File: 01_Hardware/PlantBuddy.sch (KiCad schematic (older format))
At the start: 38 parts, among them J101 Debug, J102 NFC Antenna, J2 Conn_I2C_SDA, J3 Conn_I2C_SCL, Q101 AO3401A, U101 nRF52832-QFxx, U102 LTR-303ALS-01, U6 SHTC3, Y1 32MHz, Y2 32kHz

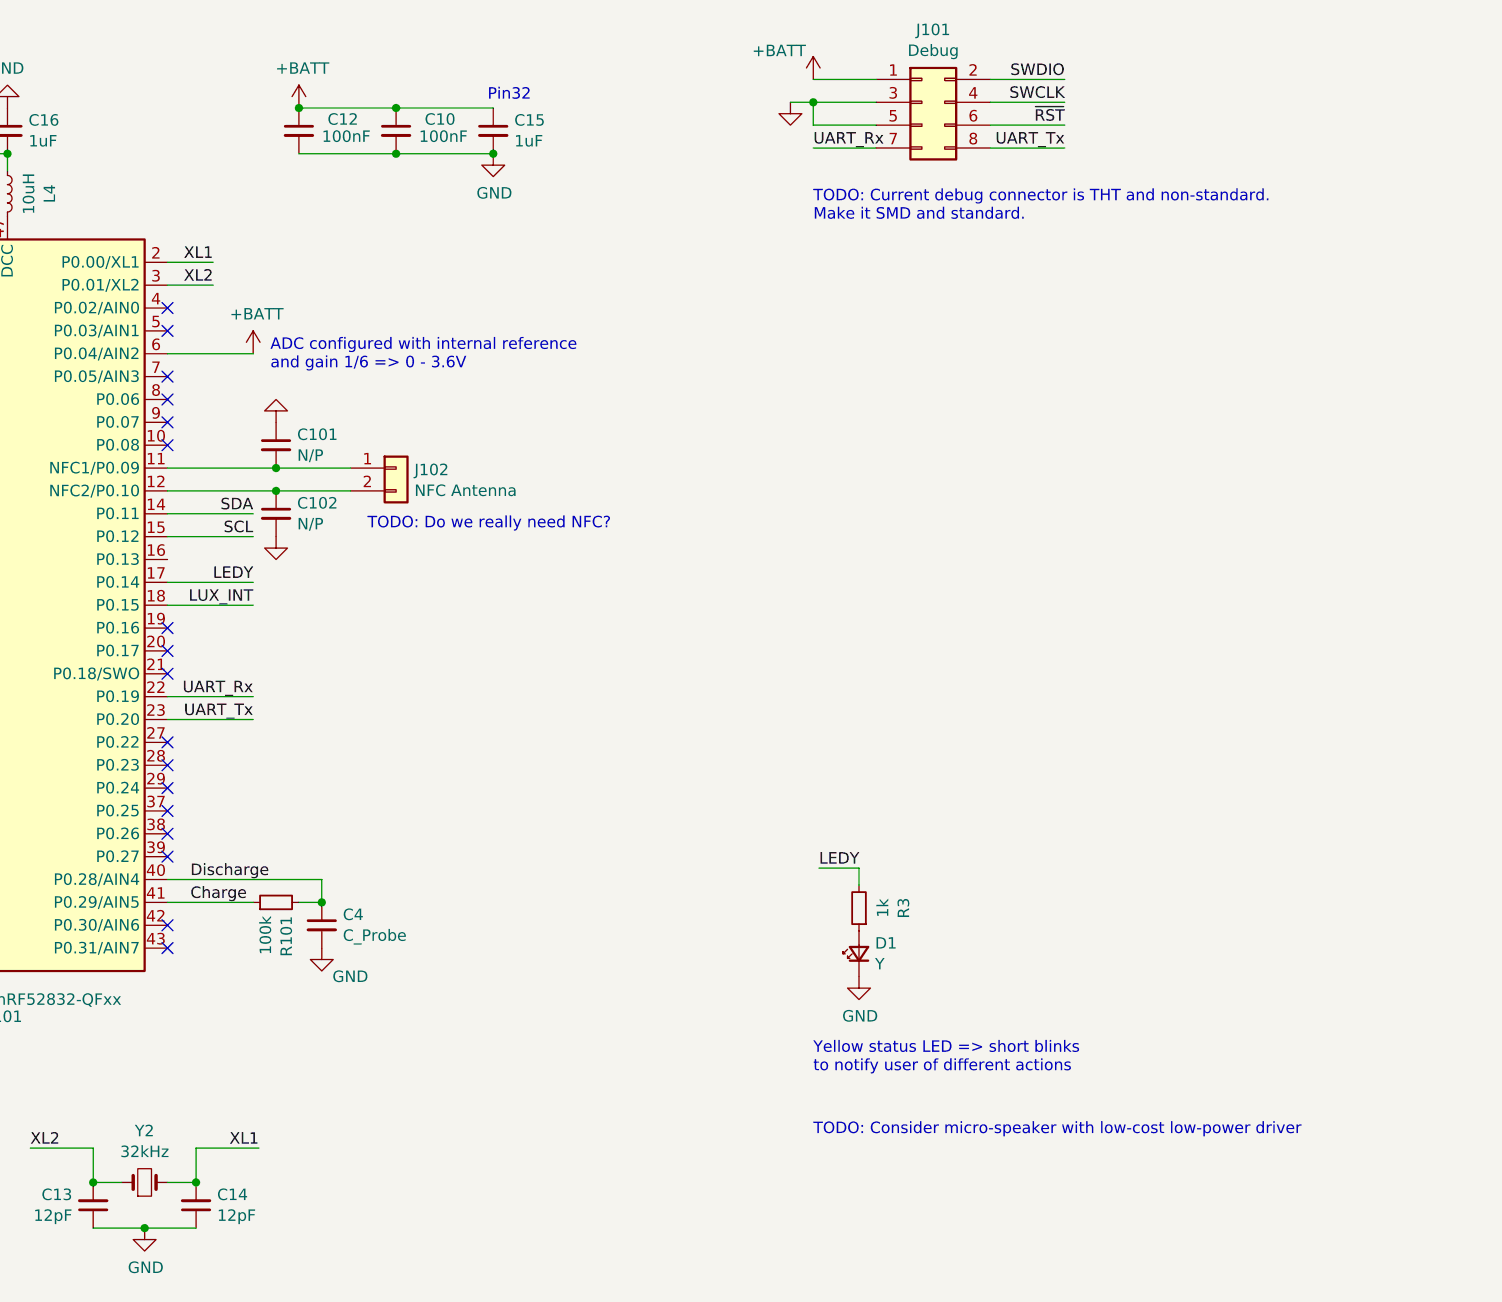
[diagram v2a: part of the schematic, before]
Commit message: Added new debug connector for J-Link.
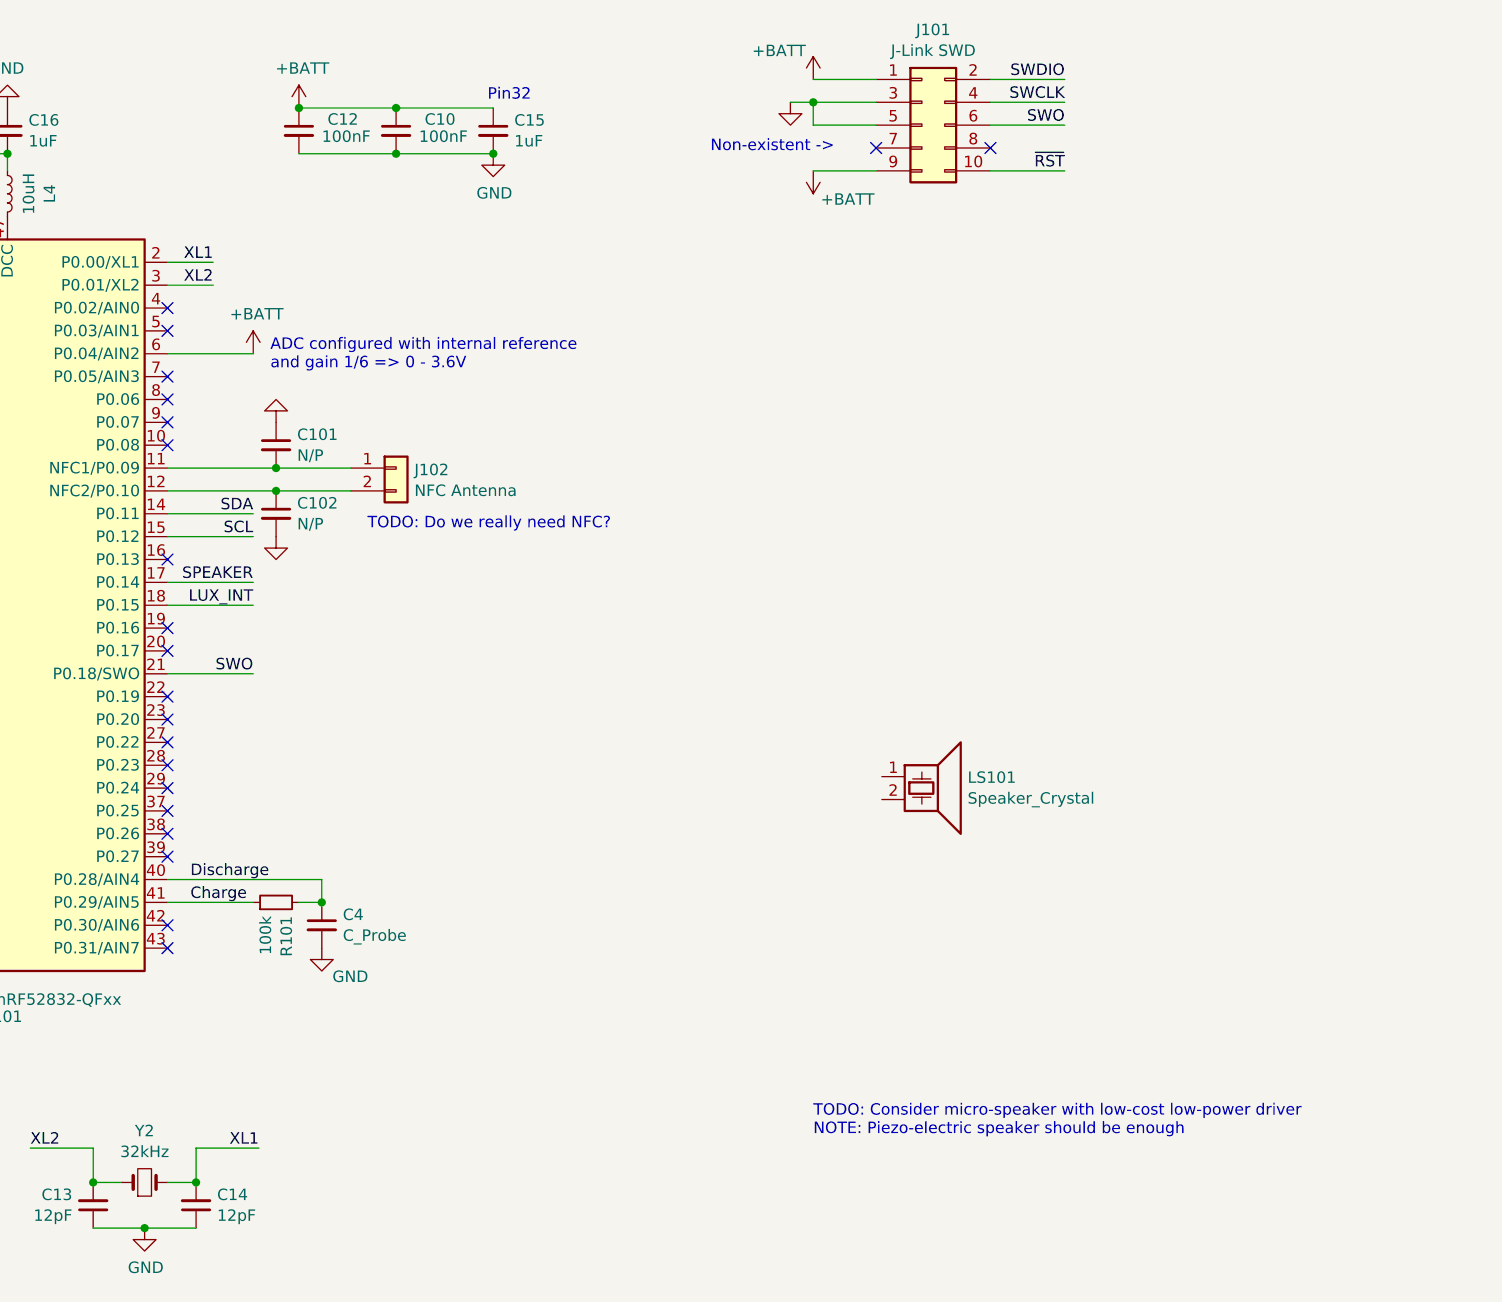
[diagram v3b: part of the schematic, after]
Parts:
- removed D1: Y, LED_SMD:LED_0603_1608Metric, symbol PlantBuddy-rescue:LED_Small-Device
- removed J101: Debug, PlantBuddy:PinHeader_2x04_P1.27mm_Vertical, symbol Connector_Generic:Conn_02x04_Odd_Even
- removed R3: 1k, Resistor_SMD:R_0402_1005Metric, symbol PlantBuddy-rescue:R_Small-Device
- added J101: J-Link SWD, Connector_PinHeader_1.27mm:PinHeader_2x05_P1.27mm_Vertical_SMD, symbol Connector_Generic:Conn_02x05_Odd_Even
- added LS101: Speaker_Crystal, symbol Device:Speaker_Crystal
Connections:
- net +BATT: now also J101.1 (Pin_1), J101.9 (Pin_9)
- net GND: now also J101.3 (Pin_3), J101.5 (Pin_5)
- net SWCLK: now also J101.4 (Pin_4)
- net SWDIO: now also J101.2 (Pin_2)
- net ~RST: now also J101.10 (Pin_10)
- net SWO: now reaches U101.21 (P0.18/SWO)
- net SWO: now also J101.6 (Pin_6)
- net LEDY renamed SPEAKER
- net UART_Rx: no longer names the net of U101.22 (P0.19)
- net UART_Tx: no longer names the net of U101.23 (P0.20)
- no-connect marks 20 -> 24
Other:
- note added: "Non-existent ->"
- note added: "TODO: Consider micro-speaker with low-cost low-power driver\nNOTE: Piezo-electric speaker should be enough"
- note removed: "TODO: Consider micro-speaker with low-cost low-power driver"
- note removed: "TODO: Current debug connector is THT and non-standard.\nMake it SMD and standard."
- note removed: "Yellow status LED => short blinks\nto notify user of different actions"
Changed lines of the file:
@@
 Text Notes 2825 7675 0    50   ~ 0
 Reverse-voltage protection
-Text Notes 9825 5225 0    50   ~ 0
-Yellow status LED => short blinks\nto notify user of different actions
 $Comp
 L PlantBuddy-rescue:Conn_01x01-Connector_Generic J3
@@
 $EndComp
 $Comp
-L PlantBuddy-rescue:LED_Small-Device D1
-U 1 1 5FC270B5
-P 10025 4700
-F 0 "D1" V 10071 4630 50  0000 R CNN
-F 1 "Y" V 9980 4630 50  0000 R CNN
-F 2 "LED_SMD:LED_0603_1608Metric" V 10025 4700 50  0001 C CNN
-F 3 "~" V 10025 4700 50  0001 C CNN
-F 4 "C72038" V 10025 4700 50  0001 C CNN "LCSC"
-	1    10025 4700
-	0    -1   -1   0
-$EndComp
-$Comp
-L PlantBuddy-rescue:GND-power #PWR01
-U 1 1 5FC2781D
-P 10025 4800
-F 0 "#PWR01" H 10025 4550 50  0001 C CNN
-F 1 "GND" H 10030 4627 50  0000 C CNN
-F 2 "" H 10025 4800 50  0001 C CNN
-F 3 "" H 10025 4800 50  0001 C CNN
-	1    10025 4800
-	1    0    0    -1
-$EndComp
-$Comp
-L PlantBuddy-rescue:R_Small-Device R3
-U 1 1 5FC33886
-P 10025 4500
-F 0 "R3" V 9829 4500 50  0000 C CNN
-F 1 "1k" V 9920 4500 50  0000 C CNN
-F 2 "Resistor_SMD:R_0402_1005Metric" H 10025 4500 50  0001 C CNN
-F 3 "~" H 10025 4500 50  0001 C CNN
-F 4 "C11702" V 10025 4500 50  0001 C CNN "LCSC"
-	1    10025 4500
-	-1   0    0    1
-$EndComp
-Wire Wire Line
-	10025 4400 10025 4325
-Wire Wire Line
-	10025 4325 9850 4325
-Text Label 9850 4325 0    50   ~ 0
-LEDY
-$Comp
 L PlantBuddy-rescue:C_Small-Device C17
 U 1 1 60156A34
@@
 Wire Wire Line
 	2875 7200 2875 7300
-Text Label 10925 1075 2    50   ~ 0
+Text Label 10925 1275 2    50   ~ 0
 ~RST
 Text Label 10925 875  2    50   ~ 0
@@
 	7375 3075 7000 3075
 Wire Wire Line
-	7375 3675 7000 3675
-Wire Wire Line
-	7375 3575 7000 3575
-Wire Wire Line
 	7000 2875 7375 2875
 Wire Wire Line
@@
 	-1   0    0    -1
 $EndComp
-Text Label 7375 3675 2    50   ~ 0
-UART_Tx
-Text Label 7375 3575 2    50   ~ 0
-UART_Rx
 Text Notes 7450 2150 0    50   ~ 0
 ADC configured with internal reference\nand gain 1/6 => 0 - 3.6V
@@
 	7375 3175 7000 3175
 Text Label 7375 3075 2    50   ~ 0
-LEDY
+SPEAKER
 Text Label 7375 3175 2    50   ~ 0
 LUX_INT
@@
 Wire Wire Line
 	10600 975  10925 975
-Text Label 10925 1175 2    50   ~ 0
-UART_Tx
-Wire Wire Line
-	10600 1175 10925 1175
-Wire Wire Line
-	10600 1075 10925 1075
+Wire Wire Line
+	10600 1275 10925 1275
 Wire Wire Line
 	7575 4475 7675 4475
@@
 NoConn ~ 7000 3875
 NoConn ~ 7000 3775
-NoConn ~ 7000 3475
 NoConn ~ 7000 3375
 NoConn ~ 7000 3275
@@
 F 3 "" H 9725 975 50  0001 C CNN
 	1    9725 975
-	1    0    0    -1
-$EndComp
-Text Label 9825 1175 0    50   ~ 0
-UART_Rx
-Wire Wire Line
-	9825 1175 10100 1175
-$Comp
-L Connector_Generic:Conn_02x04_Odd_Even J101
-U 1 1 6117791F
-P 10300 975
-F 0 "J101" H 10350 1292 50  0000 C CNN
-F 1 "Debug" H 10350 1201 50  0000 C CNN
-F 2 "PlantBuddy:PinHeader_2x04_P1.27mm_Vertical" H 10300 975 50  0001 C CNN
-F 3 "~" H 10300 975 50  0001 C CNN
-	1    10300 975
 	1    0    0    -1
 $EndComp
@@
 Wire Wire Line
 	2025 6850 1800 6850
-Text Notes 9825 1500 0    50   ~ 0
-TODO: Current debug connector is THT and non-standard.\nMake it SMD and standard.
 Text Notes 9825 5500 0    50   ~ 0
-TODO: Consider micro-speaker with low-cost low-power driver
+TODO: Consider micro-speaker with low-cost low-power driver\nNOTE: Piezo-electric speaker should be enough
 $Comp
 L PlantBuddy-rescue:Battery_Cell-Device BT1
@@
 	3325 7300 3725 7300
 Connection ~ 3325 7300
+Text Notes 7875 2850 0    50   ~ 0
+TODO: Do we really need NFC?
+Text Label 10925 1075 2    50   ~ 0
+SWO
+Wire Wire Line
+	10600 1075 10925 1075
+Text Label 7375 3475 2    50   ~ 0
+SWO
+Wire Wire Line
+	7375 3475 7000 3475
+$Comp
+L Connector_Generic:Conn_02x05_Odd_Even J101
+U 1 1 6136EE02
+P 10300 1075
+F 0 "J101" H 10350 1492 50  0000 C CNN
+F 1 "J-Link SWD" H 10350 1401 50  0000 C CNN
+F 2 "Connector_PinHeader_1.27mm:PinHeader_2x05_P1.27mm_Vertical_SMD" H 10300 1075 50  0001 C CNN
+F 3 "~" H 10300 1075 50  0001 C CNN
+	1    10300 1075
+	1    0    0    -1
+$EndComp
+NoConn ~ 10600 1175
+NoConn ~ 10100 1175
+Text Notes 9375 1200 0    50   ~ 0
+Non-existent ->
+$Comp
+L PlantBuddy-rescue:+BATT-power #PWR0121
+U 1 1 6137FB50
+P 9825 1275
+F 0 "#PWR0121" H 9825 1125 50  0001 C CNN
+F 1 "+BATT" H 9675 1400 50  0000 C CNN
+F 2 "" H 9825 1275 50  0001 C CNN
+F 3 "" H 9825 1275 50  0001 C CNN
+	1    9825 1275
+	-1   0    0    1
+$EndComp
+Wire Wire Line
+	9825 1275 10100 1275
+NoConn ~ 7000 2975
+$Comp
+L Device:Speaker_Crystal LS101
+U 1 1 6138F133
+P 10325 3925
+F 0 "LS101" H 10500 3921 50  0000 L CNN
+F 1 "Speaker_Crystal" H 10500 3830 50  0000 L CNN
+F 2 "" H 10290 3875 50  0001 C CNN
+F 3 "~" H 10290 3875 50  0001 C CNN
+	1    10325 3925
+	1    0    0    -1
+$EndComp
+NoConn ~ 7000 3575
+NoConn ~ 7000 3675
 Wire Bus Line
 	2175 5325 2625 5325
 Wire Bus Line
 	2175 5325 2175 6650
-Text Notes 7875 2850 0    50   ~ 0
-TODO: Do we really need NFC?
 $EndSCHEMATC

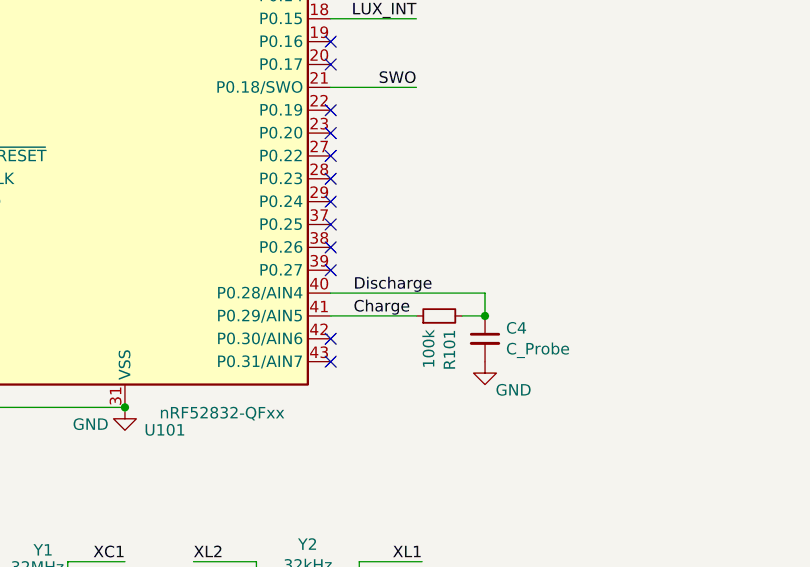
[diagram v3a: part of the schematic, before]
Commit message: PCB: Changed name of net.
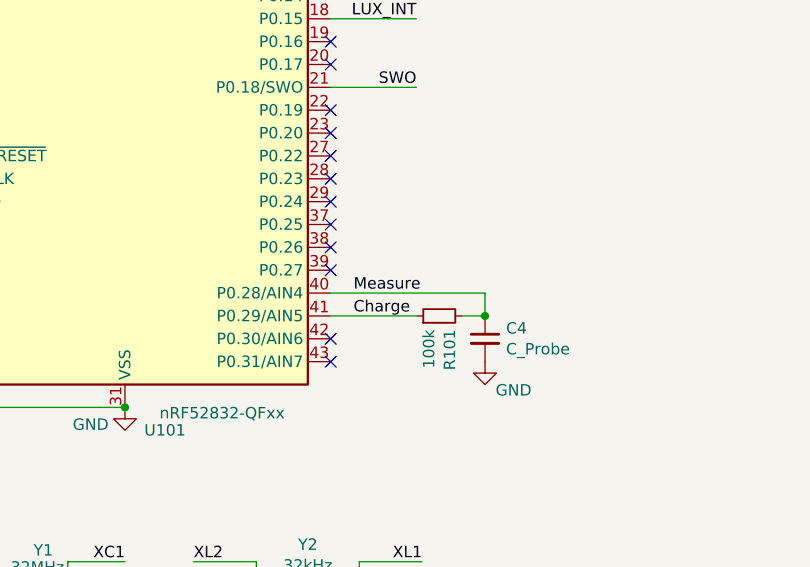
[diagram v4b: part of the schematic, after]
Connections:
- net Discharge renamed Measure
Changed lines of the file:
@@
 	7000 2775 7375 2775
 Text Label 7100 4375 0    50   ~ 0
-Discharge
+Measure
 Text Label 7100 4475 0    50   ~ 0
 Charge

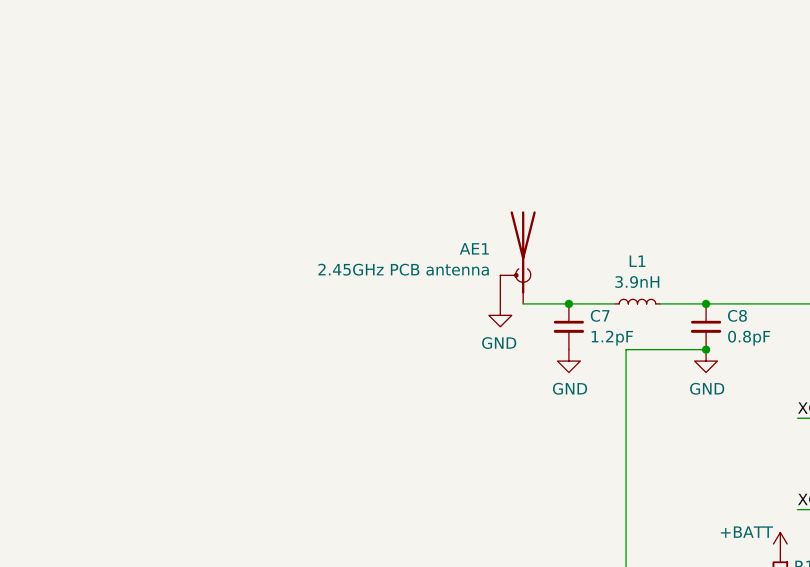
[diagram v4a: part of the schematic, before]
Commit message: Changed antenna design to monopole
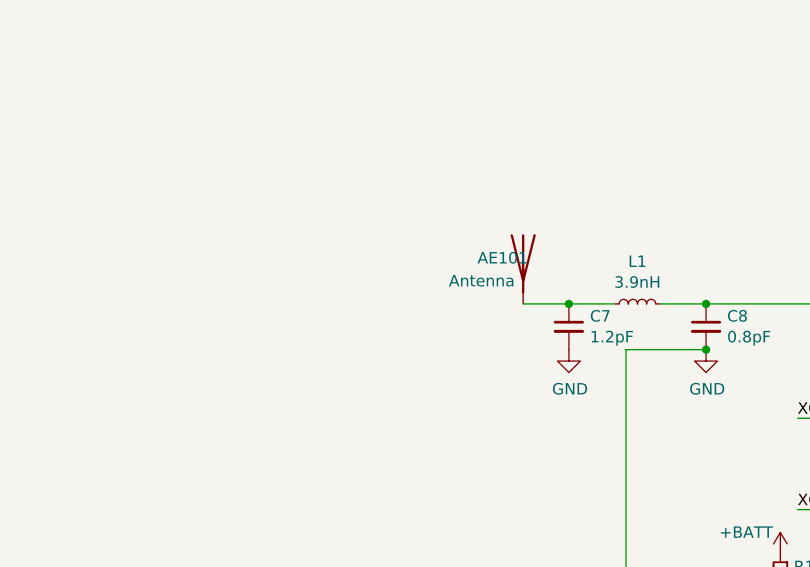
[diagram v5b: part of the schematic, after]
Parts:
- removed AE1: 2.45GHz PCB antenna, RF_Antenna:Texas_SWRA117D_2.4GHz_Right, symbol PlantBuddy-rescue:Antenna_Shield-Device
- added AE101: Antenna, PlantBuddy:monopole, symbol Device:Antenna
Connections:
- net at C7.1, L1.1: now also AE101.1 (A)
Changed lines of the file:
@@
-$EndComp
-$Comp
-L PlantBuddy-rescue:Antenna_Shield-Device AE1
-U 1 1 5F7B40C5
-P 3825 2275
-F 0 "AE1" H 3969 2314 50  0000 L CNN
-F 1 "2.45GHz PCB antenna" H 3969 2223 50  0000 L CNN
-F 2 "RF_Antenna:Texas_SWRA117D_2.4GHz_Right" H 3825 2375 50  0001 C CNN
-F 3 "~" H 3825 2375 50  0001 C CNN
-	1    3825 2275
-	-1   0    0    -1
 $EndComp
 $Comp
@@
 	1    7575 1000
 	1    0    0    -1
-$EndComp
-$Comp
-L PlantBuddy-rescue:GND-power #PWR038
-U 1 1 5F8EDD3C
-P 3725 2475
-F 0 "#PWR038" H 3725 2225 50  0001 C CNN
-F 1 "GND" H 3730 2302 50  0000 C CNN
-F 2 "" H 3725 2475 50  0001 C CNN
-F 3 "" H 3725 2475 50  0001 C CNN
-	1    3725 2475
-	-1   0    0    -1
 $EndComp
 Wire Wire Line
@@
 NoConn ~ 7000 3575
 NoConn ~ 7000 3675
+$Comp
+L Device:Antenna AE101
+U 1 1 613B6725
+P 3825 2275
+F 0 "AE101" H 3625 2275 50  0000 L CNN
+F 1 "Antenna" H 3500 2175 50  0000 L CNN
+F 2 "PlantBuddy:monopole" H 3825 2275 50  0001 C CNN
+F 3 "~" H 3825 2275 50  0001 C CNN
+	1    3825 2275
+	1    0    0    -1
+$EndComp
 Wire Bus Line
 	2175 5325 2625 5325
